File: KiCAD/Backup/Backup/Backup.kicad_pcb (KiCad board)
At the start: 2 copper layers, 75 x 140 mm, 5 parts, among them U1 NUCLEO144-F746ZG

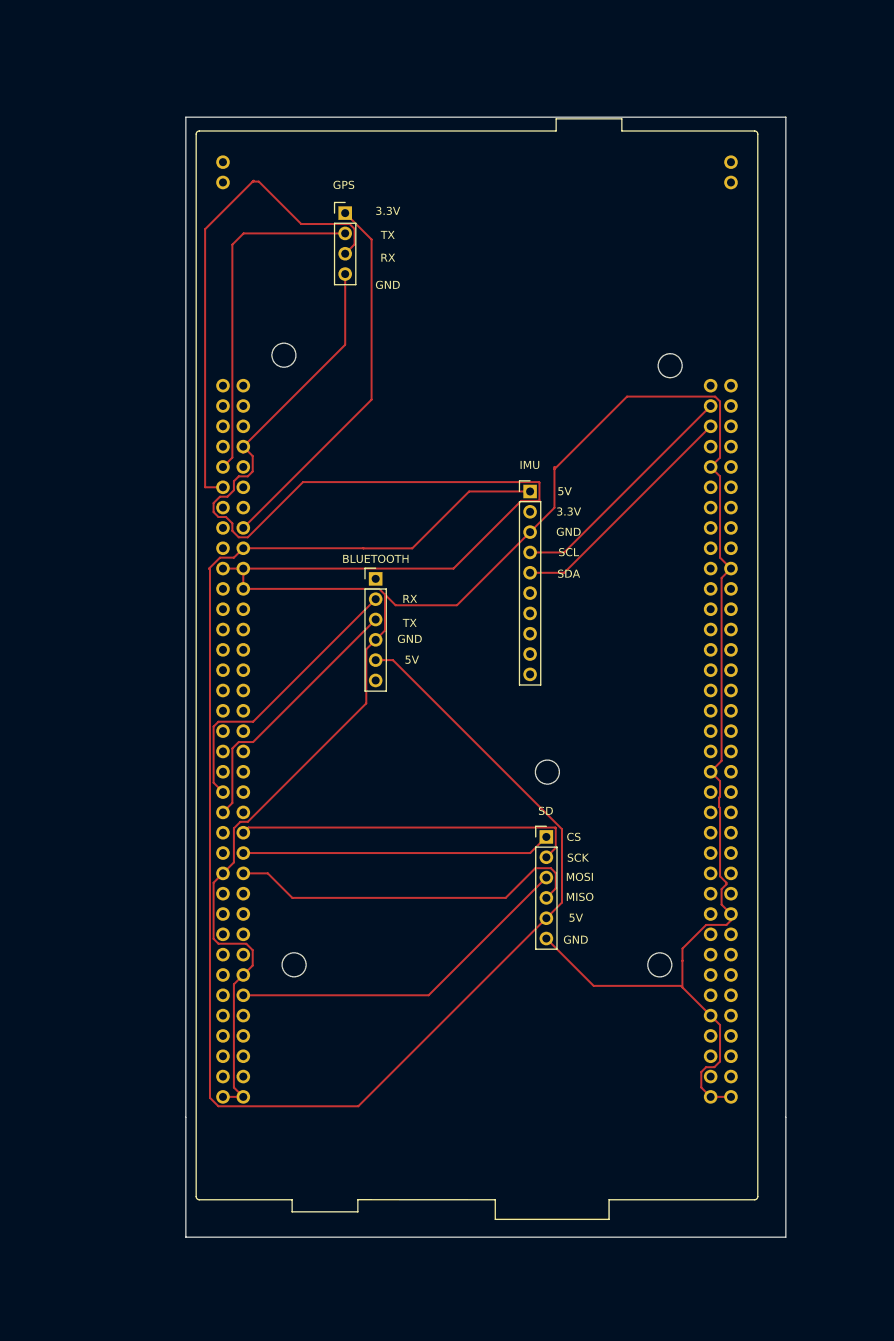
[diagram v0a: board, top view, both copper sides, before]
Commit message: update uart class
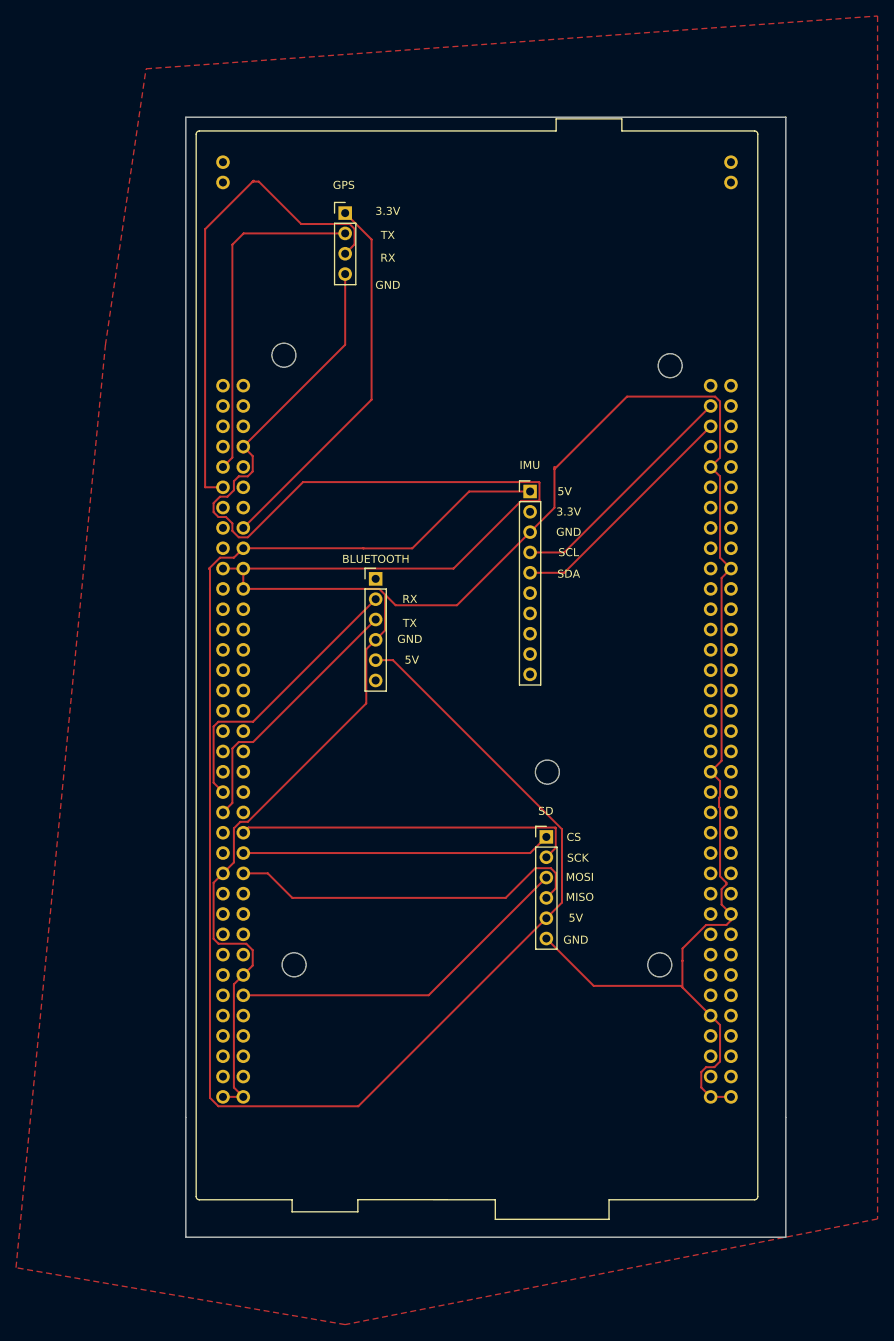
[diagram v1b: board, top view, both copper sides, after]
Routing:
- added copper zone on F.Cu, net (none)
